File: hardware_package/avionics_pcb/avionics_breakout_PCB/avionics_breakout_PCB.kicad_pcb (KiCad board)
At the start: 2 copper layers, 98 x 27.9 mm, 19 parts, among them J0 GPS, J1 ANT, J2 SER_1, J3 SER_2, J4 IGN_1, J5 IGN_2, J6 IGN_3, J7 IGN_4, J8 3V3_IN, J9 GND_IN, SW1 SW_Push

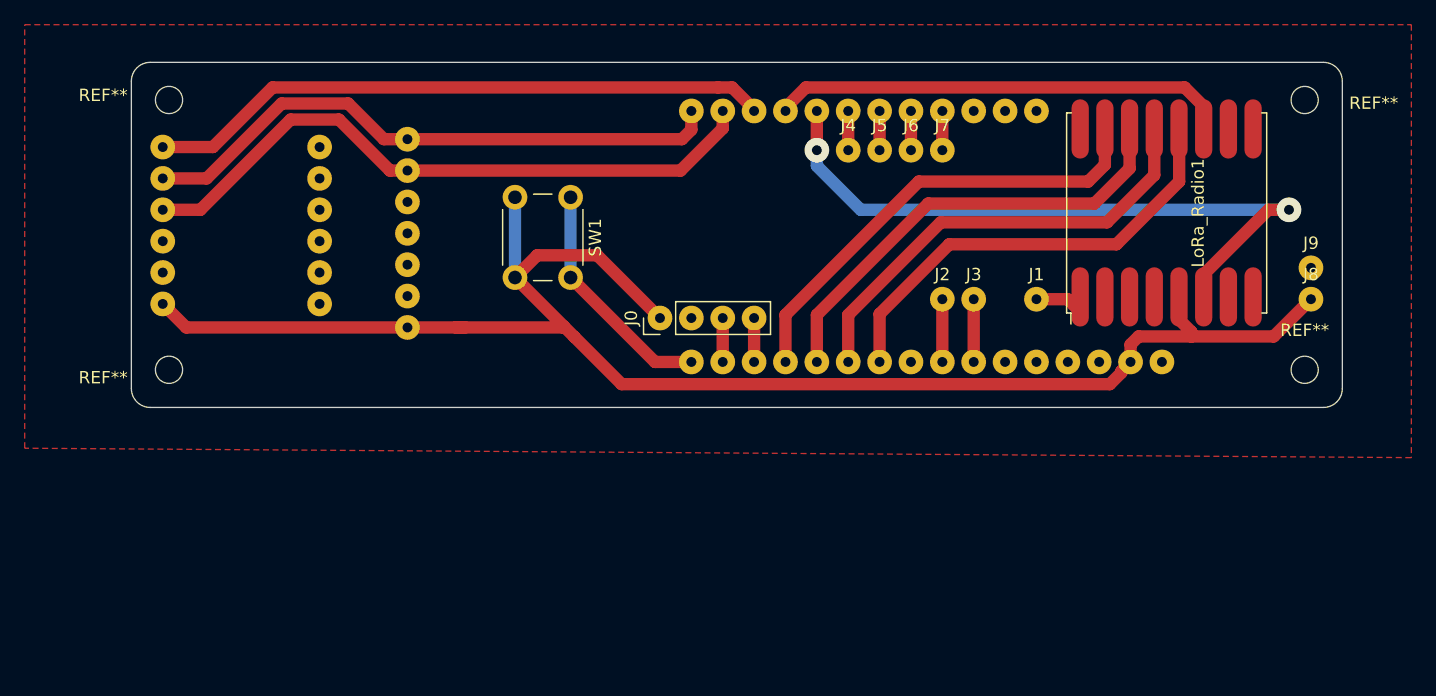
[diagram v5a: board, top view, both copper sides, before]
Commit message: Finished the new PCB layout for the breakout avionics PCB
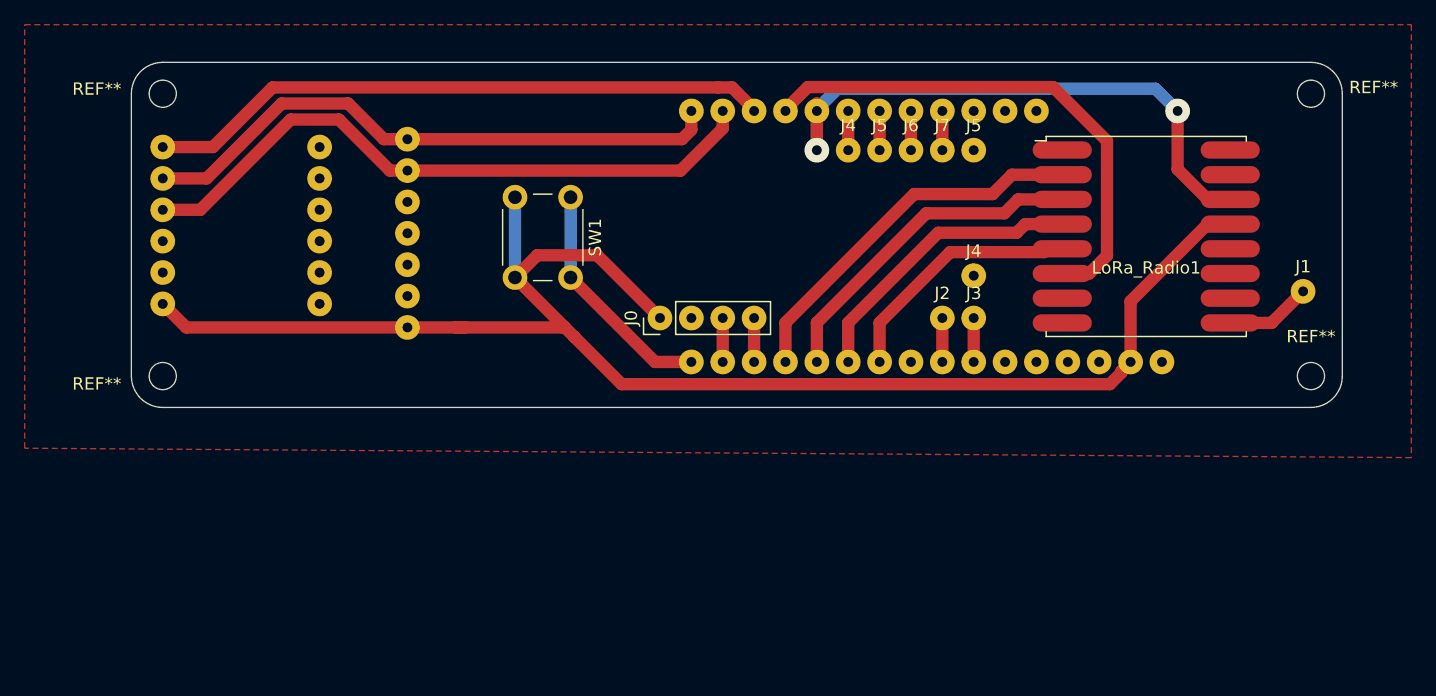
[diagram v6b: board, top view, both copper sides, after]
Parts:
- removed J8: 3V3_IN, Connector_Wire:SolderWire-0.1sqmm_1x01_D0.4mm_OD1mm
- removed J9: GND_IN, Connector_Wire:SolderWire-0.1sqmm_1x01_D0.4mm_OD1mm
- added J4: GND, Connector_Wire:SolderWire-0.1sqmm_1x01_D0.4mm_OD1mm, F.Cu at (102.2, 104.1)
- added J5: GND, Connector_Wire:SolderWire-0.1sqmm_1x01_D0.4mm_OD1mm, F.Cu at (102.2, 94.0)
- moved J1 21.6 mm to (128.9, 105.4)
- moved LoRa_Radio1 2.52 mm to (116.2, 101.0), turned to 0 degrees
- moved J2 1.52 mm to (99.7, 107.6)
- moved J3 1.52 mm to (102.2, 107.6)
- moved REF** 0.72 mm to (36.6, 89.4)
- moved REF** 0.72 mm to (36.6, 112.3)
- moved REF** 0.72 mm to (129.5, 89.4)
- moved REF** 0.72 mm to (129.5, 112.3)
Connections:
- Barometer1 pad 3: Net-(Barometer1-Pad3) -> (no net)
- Barometer1 pad 4: Net-(Barometer1-Pad4) -> (no net)
- Barometer1 pad 5: Net-(Barometer1-Pad5) -> (no net)
- IMU1 pad 10: Net-(IMU1-Pad10) -> (no net)
- IMU1 pad 11: Net-(IMU1-Pad11) -> (no net)
- IMU1 pad 12: Net-(IMU1-Pad12) -> (no net)
- IMU1 pad 2: Net-(IMU1-Pad2) -> (no net)
- IMU1 pad 8: Net-(IMU1-Pad8) -> (no net)
- IMU1 pad 9: Net-(IMU1-Pad9) -> (no net)
- LoRa_Radio1 pad 1: Net-(J1-Pad1) -> GND
- LoRa_Radio1 pad 10: Net-(LoRa_Radio1-Pad10) -> GND
- LoRa_Radio1 pad 11: RESET -> (no net)
- LoRa_Radio1 pad 12: CS -> (no net)
- LoRa_Radio1 pad 13: SCK -> +3V3
- LoRa_Radio1 pad 14: MOSI -> INT_LORA
- LoRa_Radio1 pad 15: MISO -> (no net)
- LoRa_Radio1 pad 16: GND -> (no net)
- LoRa_Radio1 pad 2: GND -> MISO
- LoRa_Radio1 pad 3: Net-(LoRa_Radio1-Pad3) -> MOSI
- LoRa_Radio1 pad 4: Net-(LoRa_Radio1-Pad4) -> SCK
- LoRa_Radio1 pad 5: +3V3 -> CS
- LoRa_Radio1 pad 6: INT_LORA -> RESET
- LoRa_Radio1 pad 7: Net-(LoRa_Radio1-Pad7) -> (no net)
- LoRa_Radio1 pad 8: Net-(LoRa_Radio1-Pad8) -> GND
- LoRa_Radio1 pad 9: GND -> Net-(J1-Pad1)
- STM32 pad 1: Net-(STM32-Pad1) -> (no net)
- STM32 pad 26: Net-(STM32-Pad26) -> (no net)
- STM32 pad 27: Net-(STM32-Pad27) -> (no net)
- STM32 pad 28: Net-(STM32-Pad28) -> (no net)
- STM32 pad 3: Net-(STM32-Pad3) -> (no net)
- STM32 pad 5: Net-(STM32-Pad5) -> (no net)
- STM32 pad 6: Net-(STM32-Pad6) -> (no net)
- STM32 pad 9: Net-(STM32-Pad9) -> (no net)
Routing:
- net CS: track 38.0 -> 19.2 mm
- net SCK: track 38.9 -> 22.6 mm
- net MOSI: track 38.6 -> 26.1 mm
- net MISO: track 38.8 -> 29.3 mm
- net INT_LORA: track 56.4 -> 49.0 mm
- net RESET: track 36.2 -> 43.4 mm
- net GND: track 5.41 -> 0.00 mm
- net +3V3: track 129.3 -> 126.1 mm
- net Net-(J1-Pad1): track 3.96 -> 5.76 mm
- net Net-(J3-Pad1): track 5.08 -> 3.56 mm
- net Net-(J2-Pad1): track 5.08 -> 3.56 mm
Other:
- outline, holes or cut-outs redrawn

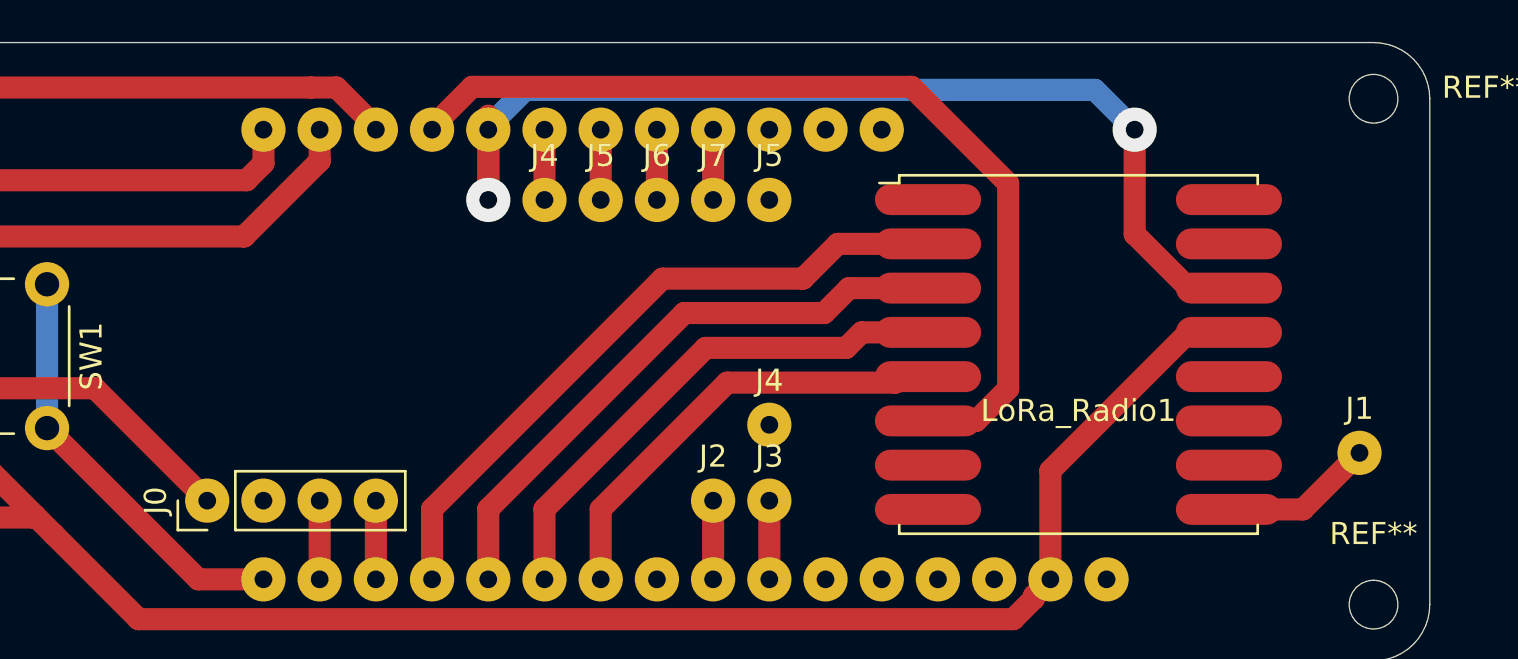
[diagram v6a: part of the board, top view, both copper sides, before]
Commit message: Update the avionics breakout PCB and schematic. These updates have made the schematic more readable, and will be used for screenshots within the readme
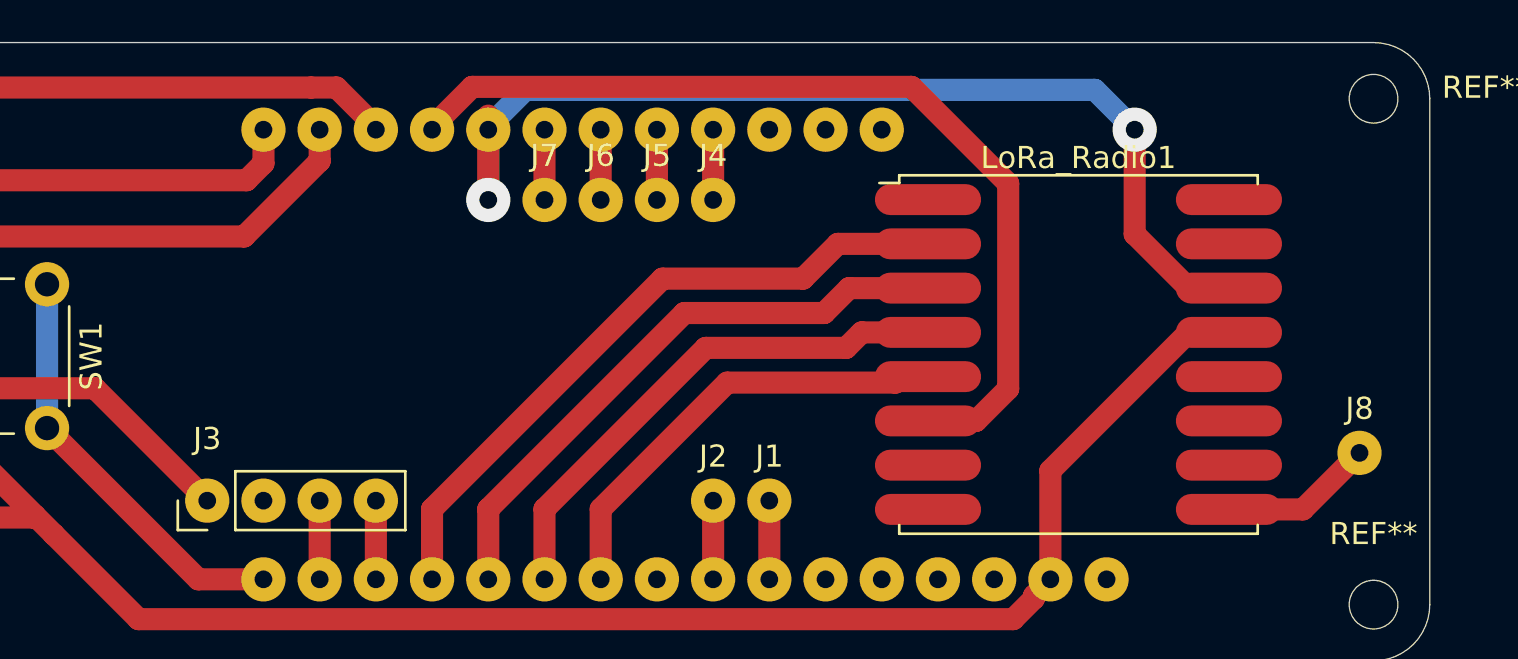
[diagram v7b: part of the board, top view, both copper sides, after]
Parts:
- removed the J4 at (102.2, 104.1)
- removed the J5 at (102.2, 94.0)
- renumbered J3 to J1, J0 to J3, J7 to J4, J6 to J5, J5 to J6, J4 to J7, J1 to J8
